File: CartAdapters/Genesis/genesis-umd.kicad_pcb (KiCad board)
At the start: 2 copper layers, 4 parts, among them CON101 UMDv2-CONN, CON102 GENESIS-CONN, U101 MCP23008T-E_SS

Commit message: genesis cart adapter work
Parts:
- C101, U101: moved to B.Cu
- moved C101 27.5 mm to (146.7, 61.9), turned to 90 degrees
- moved U101 6.75 mm to (135.9, 62.9), turned to 0 degrees
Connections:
- CON101 pad 22: /SL1 -> /~DTACK~
- CON101 pad 23: /SR1 -> /~M3~
- CON101 pad 24: Net-(CON101-Pad24) -> /~TIME~
- CON101 pad 25: Net-(CON101-Pad25) -> /~CE~
- CON101 pad 39: /~CE~ -> /~ASEL~
- CON101 pad 59: /~TIME~ -> /~AS~
- CON102 pad B1: /SL1 -> Net-(CON102-PadB1)
- CON102 pad B18: Net-(CON102-PadB18) -> /~AS~
- CON102 pad B26: Net-(CON102-PadB26) -> /~ASEL~
- CON102 pad B3: /SR1 -> Net-(CON102-PadB3)
- CON102 pad B30: Net-(CON102-PadB30) -> /~M3~
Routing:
- net /A21: track 0.00 -> 58.8 mm
- net /A5: track 0.00 -> 55.4 mm, vias 0 -> 1
- net /A6: track 0.00 -> 45.3 mm
- net /A4: track 0.00 -> 42.7 mm
- net /A2: track 0.00 -> 35.1 mm
- net /~CE~: track 0.00 -> 26.9 mm
- net /A9: track 0.00 -> 25.4 mm
- net GND: track 0.00 -> 21.6 mm
- net /~M3~: track 0.00 -> 20.5 mm
- net /~TIME~: track 0.00 -> 19.9 mm
- net +3V3: track 0.00 -> 15.8 mm
- net /A16: track 0.00 -> 15.3 mm
- net /D8: track 0.00 -> 12.3 mm
- net /D6: track 0.00 -> 12.3 mm
- net /A14: track 0.00 -> 11.5 mm
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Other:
- board outline added: 23.5 x 94.6 mm
- net class Default: clearance 0.2 -> 0.1778; trace_width 0.25 -> 0.1778; via_dia 0.8 -> 0.508; via_drill 0.4 -> 0.254
- net class Power added: clearance 0.1778, trace_width 0.254, via_dia 0.508, via_drill 0.254
- rule trace_clearance: 0.2 -> 0.1778
- rule trace_min: 0.2 -> 0.1778
- rule via_min_drill: 0.3 -> 0.254
- rule via_min_size: 0.4 -> 0.508

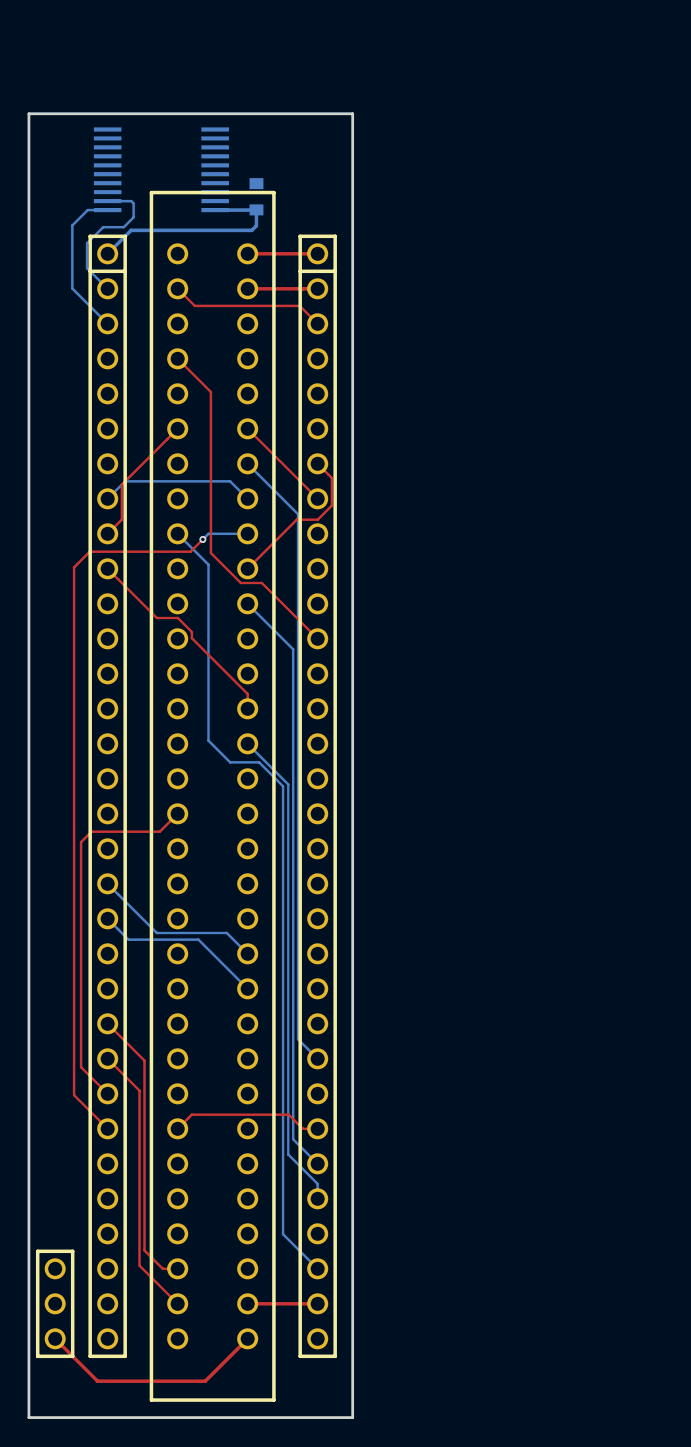
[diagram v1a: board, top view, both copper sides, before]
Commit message: increased spacing on UMDv2 connector
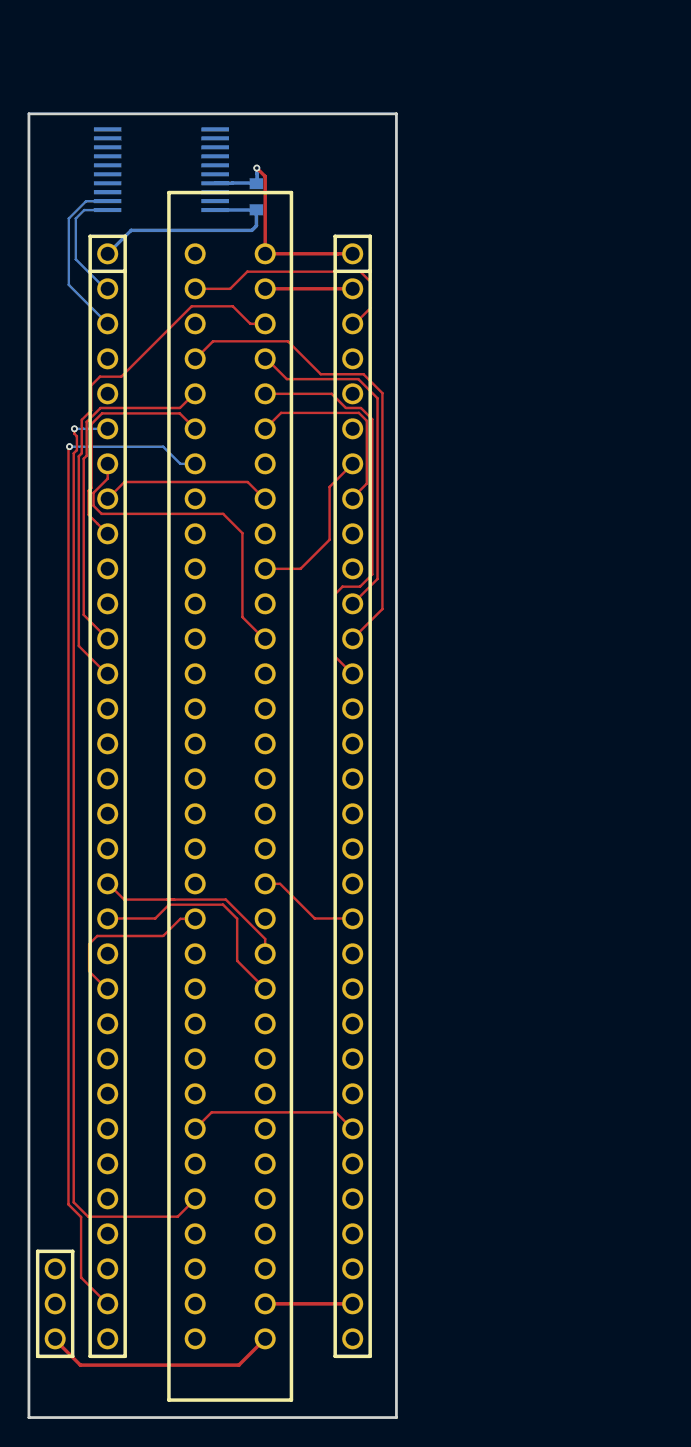
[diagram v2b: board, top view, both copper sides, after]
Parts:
- moved CON102 1.27 mm to (142.2, 66.0)
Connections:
- CON101 pad 2: /SDA -> /SCL
- CON101 pad 3: /SCL -> /SDA
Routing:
- net /A19: track 0.00 -> 73.0 mm, vias 0 -> 1
- net /~LWR~: track 0.00 -> 68.5 mm, vias 0 -> 1
- net /A21: track 58.8 -> 0.00 mm
- net /A5: track 55.4 -> 0.00 mm, vias 1 -> 0
- net /A6: track 45.3 -> 0.00 mm
- net /A4: track 42.7 -> 0.00 mm
- net /A8: track 0.00 -> 37.7 mm
- net /A2: track 35.1 -> 0.00 mm
- net /A7: track 0.00 -> 29.5 mm
- net /~CE~: track 26.9 -> 0.00 mm
- net /A10: track 0.00 -> 25.2 mm
- net /A11: track 0.00 -> 24.9 mm
- net /A15: track 0.00 -> 23.5 mm
- net /~M3~: track 20.5 -> 0.00 mm
- net /~TIME~: track 19.9 -> 0.00 mm
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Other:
- board size 23.5 x 94.6 mm -> 26.7 x 94.6 mm

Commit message: bit of routing on genesis adapter
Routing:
- net /A20: track 0.00 -> 68.5 mm, vias 0 -> 1
- net /A23: track 0.00 -> 65.6 mm, vias 0 -> 1
- net /~TIME~: track 0.00 -> 30.1 mm, vias 0 -> 1
- net /A19: track 73.0 -> 76.7 mm
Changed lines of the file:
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@@
     (thickness 1.6)
     (drawings 4)
-    (tracks 153)
+    (tracks 199)
     (zones 0)
     (modules 4)
@@
   (segment (start 140.347699 113.271299) (end 139.344398 114.2746) (width 0.1778) (layer F.Cu) (net 21))
   (segment (start 139.344398 114.2746) (end 135.8646 114.2746) (width 0.1778) (layer F.Cu) (net 21))
-  (segment (start 141.16237 81.28) (end 139.91777 80.0354) (width 0.1778) (layer B.Cu) (net 28))
+  (segment (start 135.89 139.7) (end 135.128001 138.938001) (width 0.1778) (layer F.Cu) (net 27))
+  (segment (start 135.128001 138.938001) (end 134.467601 138.938001) (width 0.1778) (layer F.Cu) (net 27))
+  (segment (start 132.156199 136.626599) (end 132.156199 126.492) (width 0.1778) (layer F.Cu) (net 27))
+  (segment (start 134.467601 138.938001) (end 132.156199 136.626599) (width 0.1778) (layer F.Cu) (net 27))
+  (segment (start 132.156199 126.492) (end 132.156199 125.044201) (width 0.1778) (layer F.Cu) (net 27))
+  (segment (start 132.156199 125.044201) (end 132.156199 125.018801) (width 0.1778) (layer F.Cu) (net 27))
+  (segment (start 132.156199 125.018801) (end 132.5118 124.6632) (width 0.1778) (layer F.Cu) (net 27))
+  (segment (start 132.5118 124.6632) (end 132.5118 124.2568) (width 0.1778) (layer F.Cu) (net 27))
+  (segment (start 132.5118 124.2568) (end 131.8006 123.5456) (width 0.1778) (layer F.Cu) (net 27))
+  (segment (start 131.8006 123.5456) (end 131.8006 93.3704) (width 0.1778) (layer F.Cu) (net 27))
+  (segment (start 131.8006 93.3704) (end 132.1308 93.0402) (width 0.1778) (layer F.Cu) (net 27))
+  (segment (start 132.1308 93.0402) (end 132.130798 92.33409) (width 0.1778) (layer F.Cu) (net 27))
+  (segment (start 132.130798 92.33409) (end 131.44501 91.648302) (width 0.1778) (layer F.Cu) (net 27))
+  (segment (start 131.44501 91.648302) (end 131.44501 85.26779) (width 0.1778) (layer F.Cu) (net 27))
+  (via (at 131.6228 85.09) (size 0.508) (drill 0.254) (layers F.Cu B.Cu) (net 27))
+  (segment (start 131.44501 85.26779) (end 131.6228 85.09) (width 0.1778) (layer F.Cu) (net 27))
+  (segment (start 131.6228 85.09) (end 141.0462 85.09) (width 0.1778) (layer B.Cu) (net 27))
+  (segment (start 141.0462 85.09) (end 142.1892 83.947) (width 0.1778) (layer B.Cu) (net 27))
   (segment (start 142.24 81.28) (end 141.16237 81.28) (width 0.1778) (layer B.Cu) (net 28))
-  (segment (start 139.91777 80.0354) (end 133.1214 80.0354) (width 0.1778) (layer B.Cu) (net 28))
-  (segment (start 133.0452 135.0264) (end 133.0452 80.1116) (width 0.1778) (layer F.Cu) (net 28))
-  (segment (start 133.9596 135.9408) (end 133.0452 135.0264) (width 0.1778) (layer F.Cu) (net 28))
-  (segment (start 133.9596 140.335) (end 133.9596 135.9408) (width 0.1778) (layer F.Cu) (net 28))
-  (segment (start 135.8392 142.2146) (end 133.9596 140.335) (width 0.1778) (layer F.Cu) (net 28))
-  (segment (start 133.0452 80.1116) (end 133.1214 80.0354) (width 0.1778) (layer F.Cu) (net 28))
-  (via (at 133.1214 80.0354) (size 0.508) (drill 0.254) (layers F.Cu B.Cu) (net 28))
+  (via (at 131.2672 80.01) (size 0.508) (drill 0.254) (layers F.Cu B.Cu) (net 28))
+  (segment (start 139.89237 80.01) (end 140.01937 80.137) (width 0.1778) (layer B.Cu) (net 28))
+  (segment (start 131.2672 80.01) (end 139.89237 80.01) (width 0.1778) (layer B.Cu) (net 28))
+  (segment (start 141.16237 81.28) (end 140.01937 80.137) (width 0.1778) (layer B.Cu) (net 28))
+  (segment (start 140.01937 80.137) (end 139.91777 80.0354) (width 0.1778) (layer B.Cu) (net 28))
+  (segment (start 131.0894 91.7956) (end 131.0894 80.645) (width 0.1778) (layer F.Cu) (net 28))
+  (segment (start 131.0894 80.645) (end 131.2672 80.4672) (width 0.1778) (layer F.Cu) (net 28))
+  (segment (start 131.775189 92.481389) (end 131.0894 91.7956) (width 0.1778) (layer F.Cu) (net 28))
+  (segment (start 134.853692 142.2146) (end 133.502387 140.863295) (width 0.1778) (layer F.Cu) (net 28))
+  (segment (start 131.444978 136.931378) (end 131.444978 93.223114) (width 0.1778) (layer F.Cu) (net 28))
+  (segment (start 135.8392 142.2146) (end 134.853692 142.2146) (width 0.1778) (layer F.Cu) (net 28))
+  (segment (start 133.502387 140.863295) (end 133.502387 138.988787) (width 0.1778) (layer F.Cu) (net 28))
+  (segment (start 133.502387 138.988787) (end 131.444978 136.931378) (width 0.1778) (layer F.Cu) (net 28))
+  (segment (start 131.2672 80.4672) (end 131.2672 80.01) (width 0.1778) (layer F.Cu) (net 28))
+  (segment (start 131.775189 92.892903) (end 131.775189 92.481389) (width 0.1778) (layer F.Cu) (net 28))
+  (segment (start 131.444978 93.223114) (end 131.775189 92.892903) (width 0.1778) (layer F.Cu) (net 28))
+  (segment (start 140.969837 92.684763) (end 131.601164 92.684763) (width 0.1778) (layer B.Cu) (net 29))
+  (segment (start 142.1892 91.4654) (end 140.969837 92.684763) (width 0.1778) (layer B.Cu) (net 29))
+  (via (at 131.241954 92.684763) (size 0.508) (drill 0.254) (layers F.Cu B.Cu) (net 29))
+  (segment (start 131.601164 92.684763) (end 131.241954 92.684763) (width 0.1778) (layer B.Cu) (net 29))
+  (segment (start 131.089367 92.83735) (end 131.241954 92.684763) (width 0.1778) (layer F.Cu) (net 29))
+  (segment (start 135.89 144.78) (end 133.146776 142.036776) (width 0.1778) (layer F.Cu) (net 29))
+  (segment (start 131.089367 137.078676) (end 131.089367 92.83735) (width 0.1778) (layer F.Cu) (net 29))
+  (segment (start 133.146776 142.036776) (end 133.146776 139.136085) (width 0.1778) (layer F.Cu) (net 29))
+  (segment (start 133.146776 139.136085) (end 131.089367 137.078676) (width 0.1778) (layer F.Cu) (net 29))
   (segment (start 147.32 68.58) (end 153.6954 68.58) (width 0.254) (layer F.Cu) (net 30))
   (segment (start 147.32 142.24) (end 153.5938 142.24) (width 0.254) (layer F.Cu) (net 30))
@@
   (segment (start 151.9936 86.7918) (end 149.8854 88.9) (width 0.1778) (layer F.Cu) (net 54))
   (segment (start 149.8854 88.9) (end 147.2946 88.9) (width 0.1778) (layer F.Cu) (net 54))
+  (segment (start 132.33761 124.46) (end 135.9154 124.46) (width 0.1778) (layer B.Cu) (net 55))
+  (via (at 131.9784 124.46) (size 0.508) (drill 0.254) (layers F.Cu B.Cu) (net 55))
+  (segment (start 131.9784 124.46) (end 132.33761 124.46) (width 0.1778) (layer B.Cu) (net 55))
+  (segment (start 134.1628 140.97) (end 133.857998 140.665198) (width 0.1778) (layer F.Cu) (net 55))
+  (segment (start 131.800589 136.773898) (end 131.800588 124.871503) (width 0.1778) (layer F.Cu) (net 55))
+  (segment (start 142.24 142.24) (end 140.97 140.97) (width 0.1778) (layer F.Cu) (net 55))
+  (segment (start 140.97 140.97) (end 134.1628 140.97) (width 0.1778) (layer F.Cu) (net 55))
+  (segment (start 133.857998 140.665198) (end 133.857998 138.831306) (width 0.1778) (layer F.Cu) (net 55))
+  (segment (start 133.857998 138.831306) (end 131.800589 136.773898) (width 0.1778) (layer F.Cu) (net 55))
+  (segment (start 131.9784 124.693691) (end 131.9784 124.46) (width 0.1778) (layer F.Cu) (net 55))
+  (segment (start 131.800588 124.871503) (end 131.9784 124.693691) (width 0.1778) (layer F.Cu) (net 55))
   (segment (start 142.24 68.58) (end 144.78 68.58) (width 0.1778) (layer F.Cu) (net 58))
   (segment (start 144.78 68.58) (end 146.0246 67.3354) (width 0.1778) (layer F.Cu) (net 58))

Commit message: bit of routing the on Genesis Adapter
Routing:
- net /A22: track 0.00 -> 61.3 mm, vias 0 -> 1
- net /~WR~: track 0.00 -> 60.8 mm, vias 0 -> 1
- net /~M3~: track 0.00 -> 30.8 mm
- net /A16: track 0.00 -> 18.9 mm
